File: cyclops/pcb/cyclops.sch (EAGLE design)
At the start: 153 parts, among them Q1 BC817, Q2 IRF510, Q3 BC817, Q4 BC817, T0 0, T1 0, T2 0, T3 0, U1 MCP4921, U10 TLV2374, U11 THS4281, U12 MAX4564, U13 ZXTD, U14 ZXTD, U2 ADG3301, U3 MAX4564, U4 LT1931, U5 LT1764A, U6 337L, U67 MCP1702, U69 LT1716, U7 TLV3701, U8 ADR03, U9 OP1177

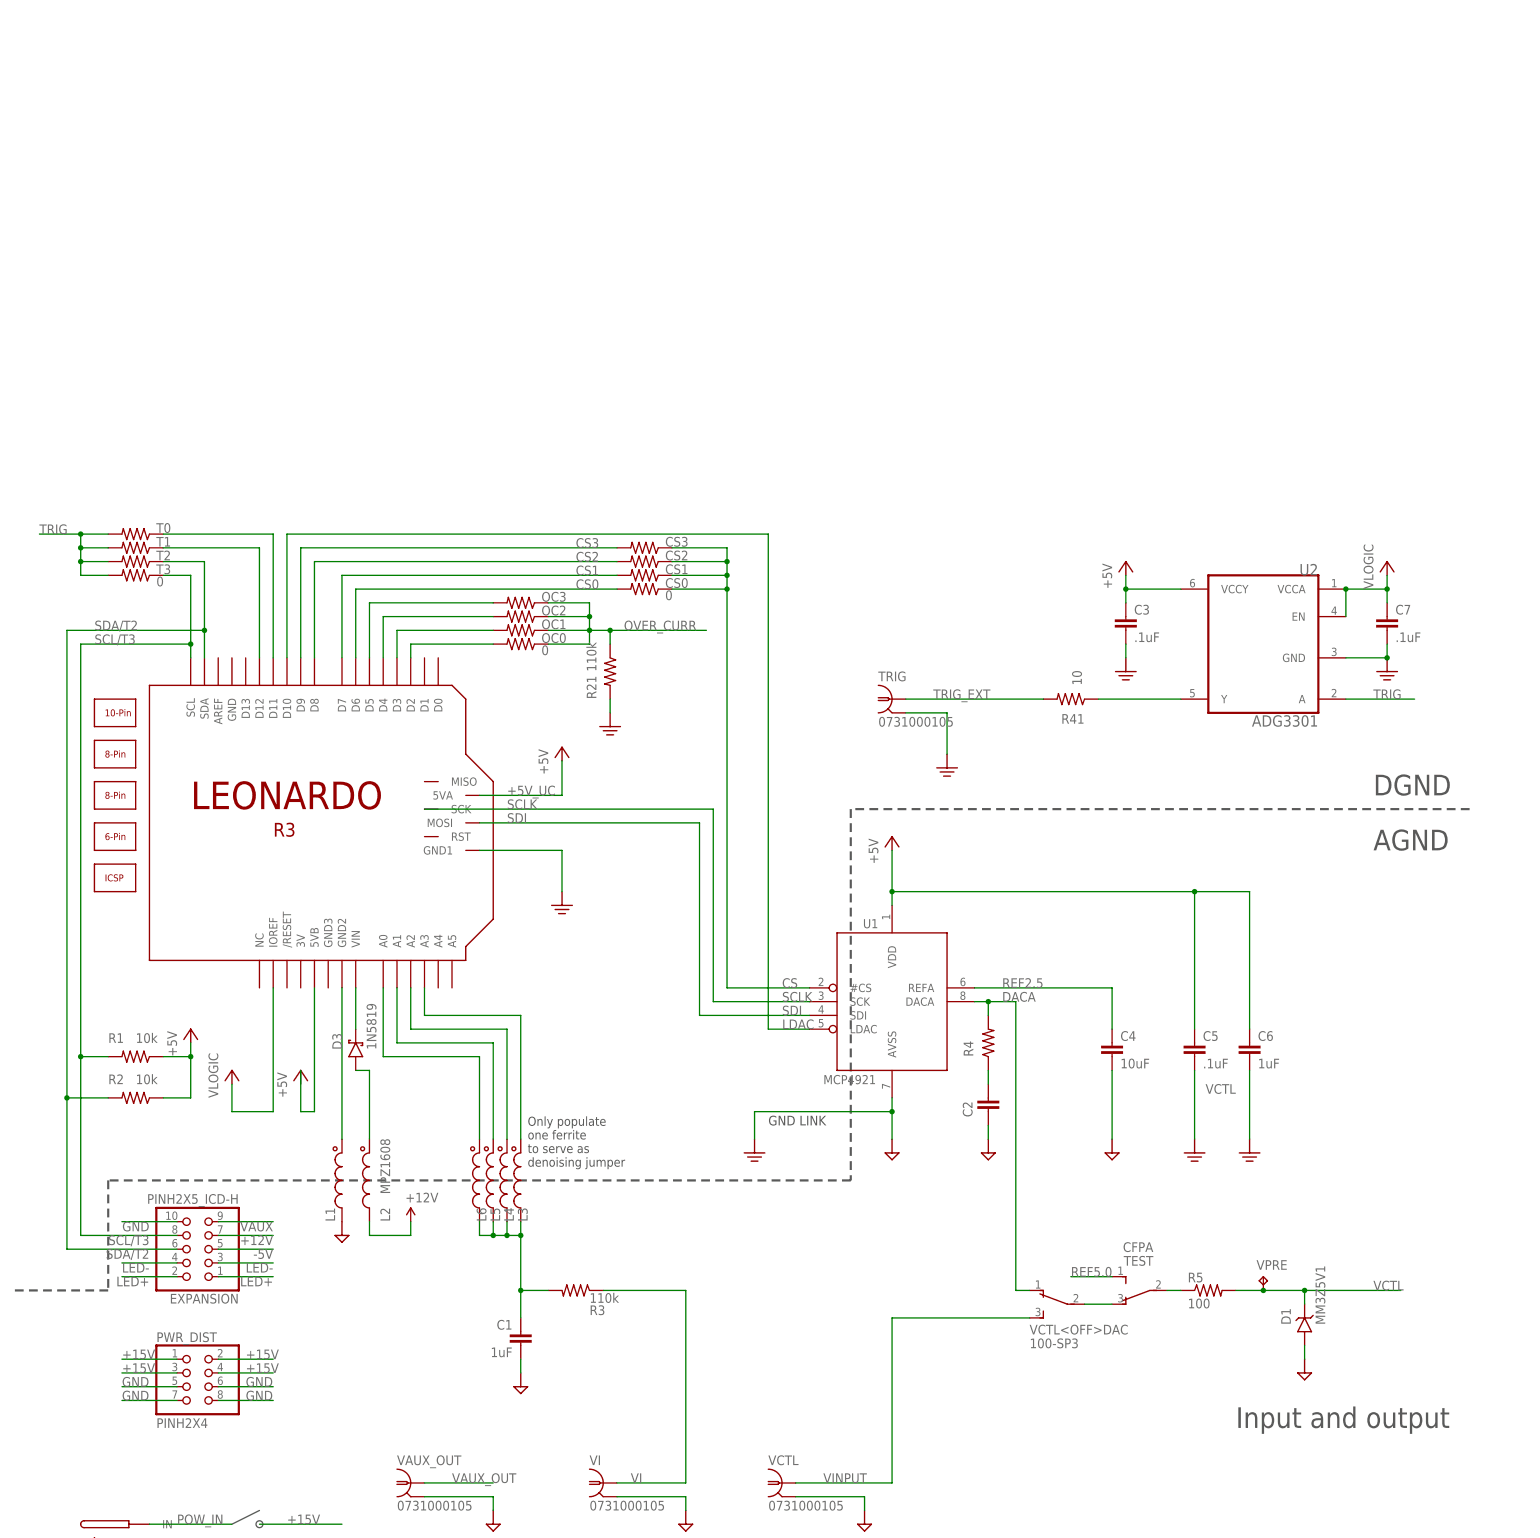
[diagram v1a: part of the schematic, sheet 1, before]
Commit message: Started Arduino --> Teensy circuit transformation
- Schematic fairly finalized
- PCB not finished. Lots of movement in panel components so this will
  require a panel redesign as well.
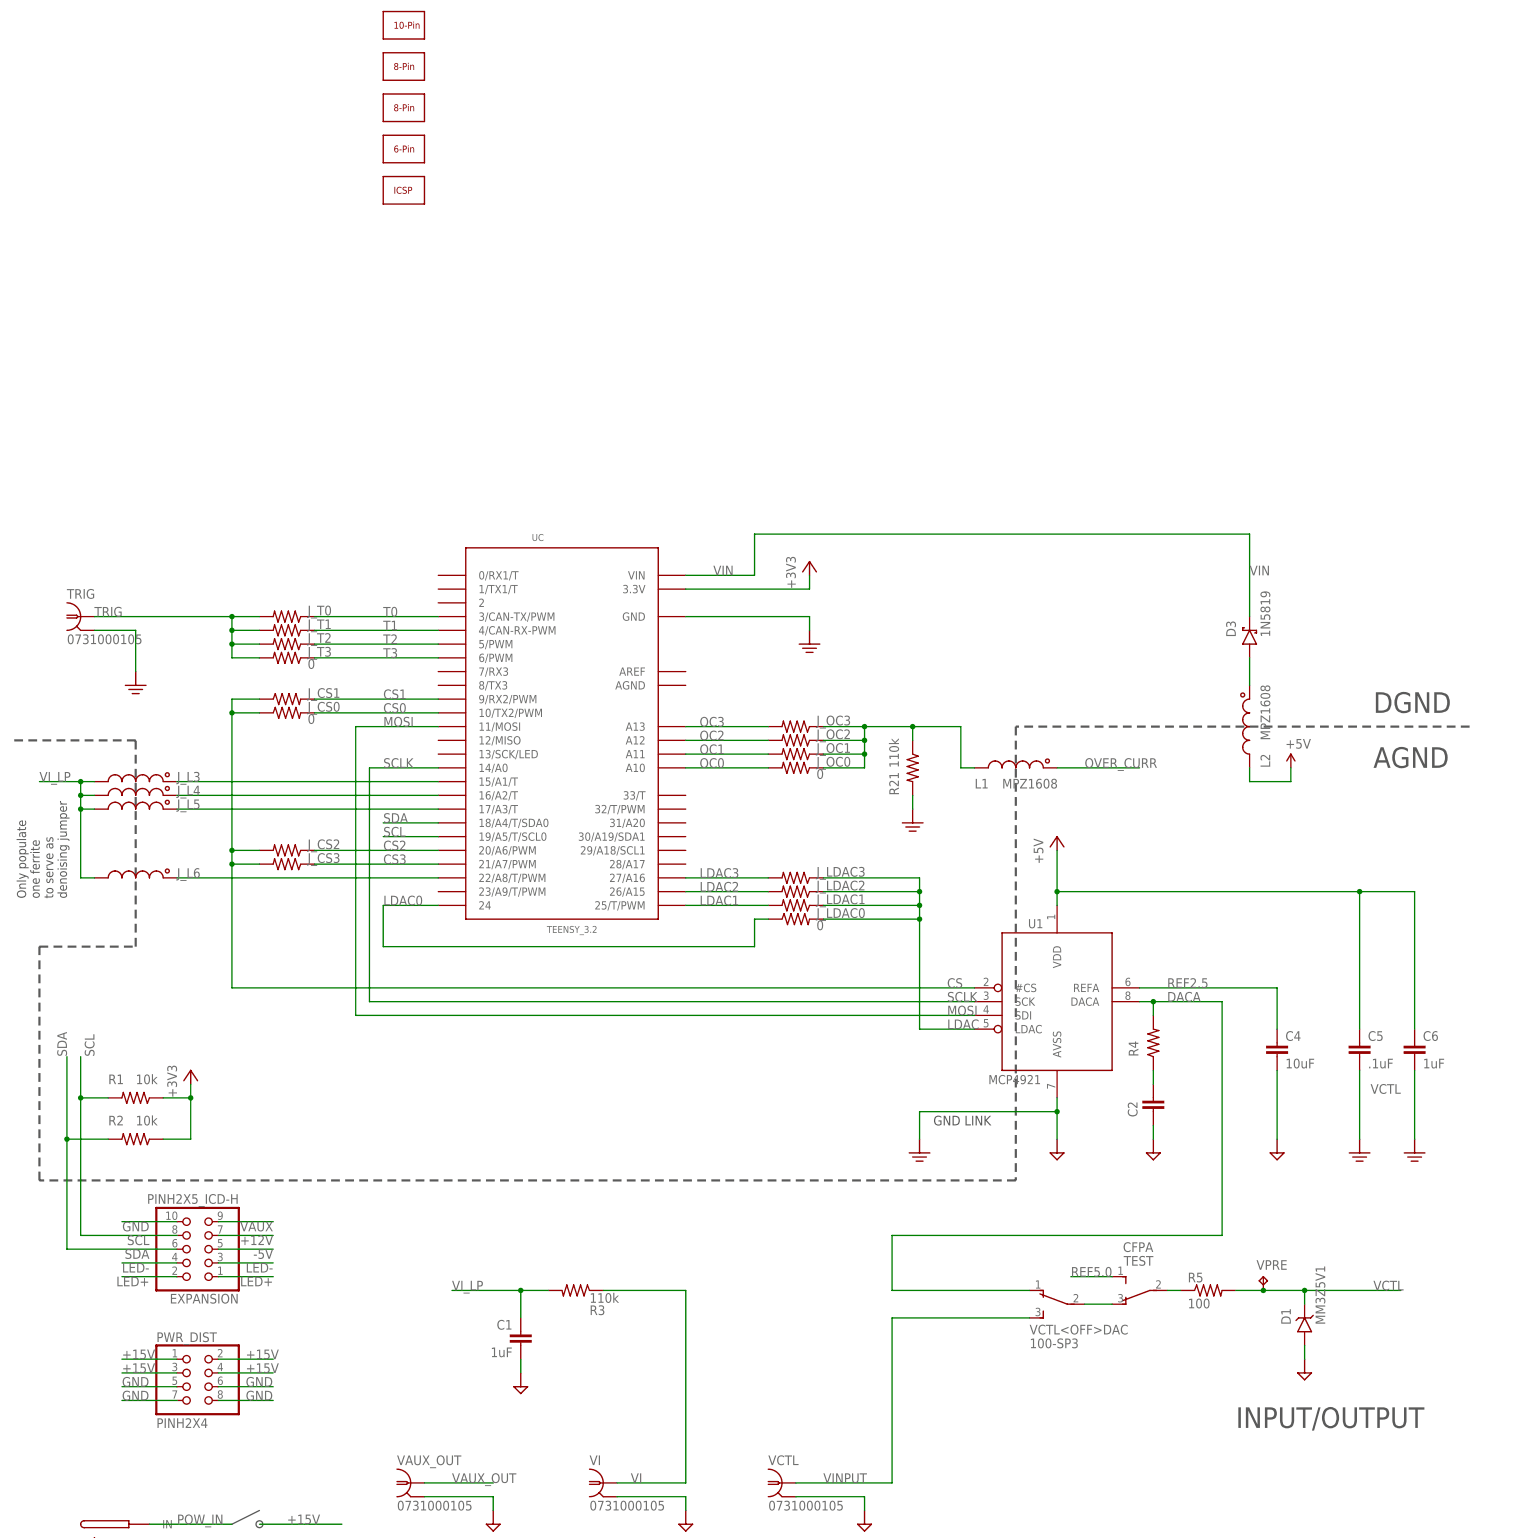
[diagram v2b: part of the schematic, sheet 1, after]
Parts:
- removed C3, C7: .1uF, cyclops:C_0603
- removed CS0, CS1, CS2, CS3, OC0, OC1, OC2, OC3, T0, T1, T2, T3: 0, cyclops:R_0603
- removed L3, L4, L5, L6: MPZ1608, cyclops:L_0603
- removed LEONARDO: LEONARDO_R3_ICSP, cyclops:LEONARDO_R3_ICSP
- removed R41: 10, cyclops:R_0603
- removed U2: ADG3301, cyclops:ADG3301BKSZ-REEL
- added J_CS0, J_CS1, J_CS2, J_CS3, J_LDAC0, J_LDAC1, J_LDAC2, J_LDAC3, J_OC0, J_OC1, J_OC2, J_OC3, J_T0, J_T1, J_T2, J_T3: 0, cyclops:R_0603
- added J_L3, J_L4, J_L5, J_L6: MPZ1608, cyclops:L_0603
- added UC: TEENSY_3.2, jonnew:TEENSY_3.1_CYCLOPS
- U67: value MCP1702 -> ZLDO1117; device jonnew:LDO-FIXED_MCP1702 -> jonnew:LDO-FIXED_SOT223
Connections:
- removed net +5V_UC: C3.1, C5.1, C6.1, LEONARDO.5VA, LEONARDO.5VB, R1.1, R2.1, U1.VDD, U2.VCCY
- removed net KEEPOUT_GND: L1.1, LEONARDO.GND2
- removed net N$11: C1.1, L3.2, L4.2, L5.2, L6.2, R3.2
- removed net N$40: LEONARDO.D2, OC0.2
- removed net N$50: R41.1, U2.Y
- removed net SCL/T3: EXPANSION.8, LEONARDO.SCL, R1.2, T3.1
- removed net SDA/T2: EXPANSION.6, LEONARDO.SDA, R2.2, T2.1
- removed net SDI: LEONARDO.MOSI, U1.SDI
- removed net TRIG_EXT: R41.2, TRIG.1
- removed net VIN_ARDUINO: C9.1, D3.C, L7G$2.2, LEONARDO.VIN, U4.VIN, U4.~SHDN
- removed net VLOGIC: C7.1, LEONARDO.IOREF, U2.EN, U2.VCCA
- new net +3V3: R1.1, R2.1, UC.3.3V
- new net LDAC0: J_LDAC0.1, UC.24
- new net LDAC1: J_LDAC1.2, UC.25/T/PWM
- new net LDAC2: J_LDAC2.2, UC.26/A15
- new net LDAC3: J_LDAC3.2, UC.27/A16
- new net MOSI: U1.SDI, UC.11/MOSI
- new net N$38: J_OC0.1, J_OC1.1, J_OC2.1, J_OC3.1, L1.2, R21.1
- new net OC3: J_OC3.2, UC.A13
- new net SCL: EXPANSION.8, R1.2, UC.19/A5/T/SCL0
- new net SDA: EXPANSION.6, R2.2, UC.18/A4/T/SDA0
- new net T2: J_T2.1, UC.5/PWM
- new net T3: J_T3.1, UC.6/PWM
- new net VIN: C9.1, D3.C, L7G$2.2, U4.VIN, U4.~SHDN, UC.VIN
- new net VI_LP: C1.1, J_L3.2, J_L4.2, J_L5.2, J_L6.2, R3.2
- net +12V: no longer L2.2
- net +5V: now also C5.1, C6.1, L2.2, U1.VDD
- net CS: now also J_CS0.1, J_CS1.1, J_CS2.2, J_CS3.2; no longer CS0.1, CS1.1, CS2.1, CS3.1
- net CS0: now also J_CS0.2, UC.10/TX2/PWM; no longer CS0.2, LEONARDO.D6
- net CS1: now also J_CS1.2, UC.9/RX2/PWM; no longer CS1.2, LEONARDO.D7
- net CS2: now also J_CS2.1, UC.20/A6/PWM; no longer CS2.2, LEONARDO.D8
- net CS3: now also J_CS3.1, UC.21/A7/PWM; no longer CS3.2, LEONARDO.D9
- net GND: now also UC.GND; no longer C3.2, C7.2, LEONARDO.GND1, U2.GND
- net LDAC: now also J_LDAC0.2, J_LDAC1.1, J_LDAC2.1, J_LDAC3.1; no longer LEONARDO.D10
- net N$19: now also J_L5.1, UC.17/A3/T; no longer L5.1, LEONARDO.A1
- net N$21: now also J_L4.1, UC.16/A2/T; no longer L4.1, LEONARDO.A2
- net N$23: now also J_L3.1, UC.15/A1/T; no longer L3.1, LEONARDO.A3
- net N$7: now also J_L6.1, UC.22/A8/T/PWM; no longer L6.1, LEONARDO.A0
- net OC0: now also J_OC0.2, UC.A10; no longer LEONARDO.D3, OC1.2
- net OC1: now also J_OC1.2, UC.A11; no longer LEONARDO.D4, OC2.2
- net OC2: now also J_OC2.2, UC.A12; no longer LEONARDO.D5, OC3.2
- net OVER_CURR: now also L1.1; no longer OC0.1, OC1.1, OC2.1, OC3.1, R21.1
- net SCLK: now also UC.14/A0; no longer LEONARDO.SCK
- net T0: now also J_T0.1, UC.3/CAN-TX/PWM; no longer LEONARDO.D11, T0.1
- net T1: now also J_T1.1, UC.4/CAN-RX-PWM; no longer LEONARDO.D12, T1.1
- net TRIG: now also J_T0.2, J_T1.2, J_T2.2, J_T3.2, TRIG.1; no longer T0.2, T1.2, T2.2, T3.2, U2.A
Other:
- note added: "INPUT/OUTPUT"
- note added: "NEG. REGULATION"
- note added: "POS. REGULATION"
- note removed: "Input and output"
- note removed: "Input offset of TLV2374 is 6.5 mV max. At unity gain, we should not get spurious triggers with a ref of 10 mV"
- note removed: "Neg. Regulation"
- note removed: "Pos. Regulation"
- moved on the sheet: C2, C4, C5, C6, D3, L1, L2, R1, R2, R21, R4, TRIG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

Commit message: More teensy layout.
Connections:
- removed net GND1: Q4.E
- net GND: now also Q4.E
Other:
- note added: "TODO: 1. Replace arduino headers with teensy headers (male and female since ttensy comes without them) 2. Are the LED arrays mounted at correct distance from board edge? 3. Is teensy at correct distance from board edge? 4. Is there adequare clearance b/w rear panel mount components 5. Rearrange panels to fit changes in front and back 6. +5V regulator layout 7. Test LED ON circuit. You will at lea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"
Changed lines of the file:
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@@
 <wire x1="15.24" y1="60.96" x2="15.24" y2="99.06" width="0.4064" layer="97" style="shortdash"/>
 <wire x1="15.24" y1="99.06" x2="-7.62" y2="99.06" width="0.4064" layer="97" style="shortdash"/>
+<text x="76.2" y="200.66" size="2.54" layer="97">TODO:
+1. Replace arduino headers with teensy headers (male and female since ttensy comes without them)
+2. Are the LED arrays mounted at correct distance from board edge?
+3. Is teensy at correct distance from board edge?
+4. Is there adequare clearance b/w rear panel mount components
+5. Rearrange panels to fit changes in front and back
+6. +5V regulator layout
+7. Test LED ON circuit. You will at least have to replace the N BJT with an P BJT since LED ON is inverted.
+8. </text>
 </plain>
 <instances>
@@
 <wire x1="-30.48" y1="-40.64" x2="-30.48" y2="-45.72" width="0.1524" layer="91"/>
 </segment>
+<segment>
+<pinref part="Q4" gate="G$1" pin="E"/>
+<wire x1="38.1" y1="-38.1" x2="38.1" y2="-60.96" width="0.1524" layer="91"/>
+</segment>
 </net>
 <net name="N$5" class="0">
@@
 </segment>
 </net>
-<net name="GND1" class="0">
-<segment>
-<pinref part="Q4" gate="G$1" pin="E"/>
-<wire x1="38.1" y1="-38.1" x2="38.1" y2="-60.96" width="0.1524" layer="91"/>
-</segment>
-</net>
